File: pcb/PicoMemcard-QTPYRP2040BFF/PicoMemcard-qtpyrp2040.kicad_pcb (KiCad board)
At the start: 2 copper layers, 36.2 x 51.2 mm, 9 parts, among them J1 PSX Memory Card Interface, SW1 TS-1187A-B-A-B, SW2 TS-1187A-B-A-B, SW3 TS-1187A-B-A-B, U1 QT_PY_SD_BFF, U2 ADAFRUIT_QT_PY

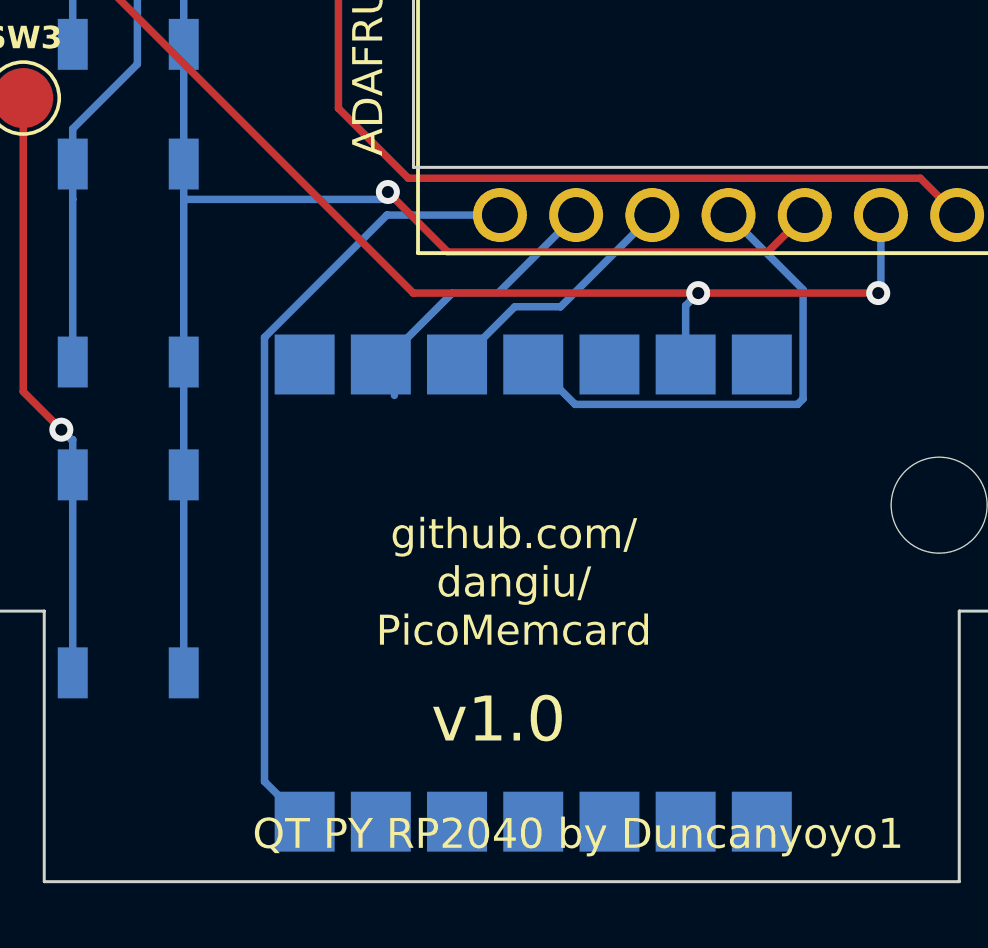
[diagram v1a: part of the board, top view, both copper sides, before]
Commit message: Connect 3V3 NET to MicroSD BFF
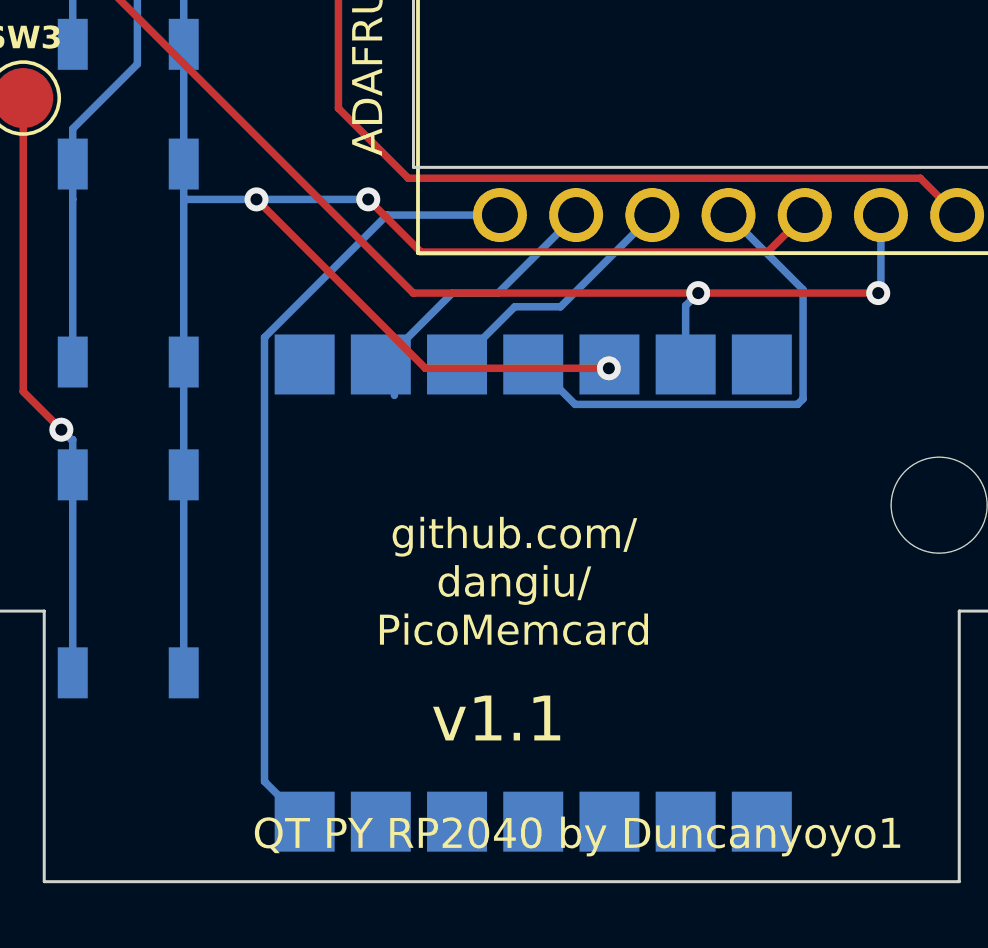
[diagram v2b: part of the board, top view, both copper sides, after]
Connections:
- U1 pad 12: +3.3V -> +3V3
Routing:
- net +3V3: track 49.7 -> 63.6 mm, vias 1 -> 3
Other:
- board text added: "v1.1"
- board text removed: "v1.0"
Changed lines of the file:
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@@
   (net 15 "MOSI")
   (net 16 "+3V3")
-  (net 17 "+3.3V")
   (footprint "MountingHole:MountingHole_3.2mm_M3" (layer "F.Cu")
     (at 163.53 102.07)
@@
     (pad "12" smd roundrect (at 7.62 2.54 90) (size 2 2) (layers "B.Cu" "B.Paste" "B.Mask") (roundrect_rratio 0.25)
       (chamfer_ratio 0) (chamfer top_left bottom_left)
-      (net 17 "+3.3V") (pinfunction "3V3") (pintype "power_in"))
+      (net 16 "+3V3") (pinfunction "3V3") (pintype "power_in"))
     (pad "13" smd roundrect (at 7.62 5.08 90) (size 2 2) (layers "B.Cu" "B.Paste" "B.Mask") (roundrect_rratio 0.25)
       (chamfer_ratio 0) (chamfer top_left bottom_left)
@@
     (effects (font (size 1 1) (thickness 0.22)))
   )
-  (gr_text "v1.0" (at 148.844 109.22) (layer "F.SilkS")
+  (gr_text "v1.1" (at 148.844 109.22) (layer "F.SilkS")
     (effects (font (size 1.5 1.5) (thickness 0.3)))
   )
@@
   (segment (start 158.994 94.8846) (end 156.509 92.3992) (width 0.25) (layer "B.Cu") (net 15))
   (segment (start 150.064 97.38) (end 150 97.38) (width 0.25) (layer "B.Cu") (net 15))
-  (segment (start 157.8149 93.6333) (end 147.1564 93.6333) (width 0.25) (layer "F.Cu") (net 16))
-  (segment (start 147.1564 93.6333) (end 145.154 91.6309) (width 0.25) (layer "F.Cu") (net 16))
-  (segment (start 159.049 92.3992) (end 157.8149 93.6333) (width 0.25) (layer "F.Cu") (net 16))
-  (via (at 145.154 91.6309) (size 0.8) (drill 0.4) (layers "F.Cu" "B.Cu") (net 16))
+  (segment (start 144.5 91.8769) (end 146.2564 93.6333) (width 0.25) (layer "F.Cu") (net 16))
+  (segment (start 140.774394 91.877634) (end 146.404406 97.507646) (width 0.25) (layer "F.Cu") (net 16))
+  (segment (start 157.8149 93.6333) (end 159.049 92.3992) (width 0.25) (layer "F.Cu") (net 16))
+  (segment (start 146.2564 93.6333) (end 157.8149 93.6333) (width 0.25) (layer "F.Cu") (net 16))
+  (segment (start 146.404406 97.507646) (end 152.520396 97.507646) (width 0.25) (layer "F.Cu") (net 16))
+  (via (at 140.774394 91.877634) (size 0.8) (drill 0.4) (layers "F.Cu" "B.Cu") (net 16))
+  (via (at 152.520396 97.507646) (size 0.8) (drill 0.4) (layers "F.Cu" "B.Cu") (net 16))
+  (via (at 144.5 91.8769) (size 0.8) (drill 0.4) (layers "F.Cu" "B.Cu") (net 16))
   (segment (start 138.35 80.11) (end 138.35 86.71) (width 0.25) (layer "B.Cu") (net 16))
+  (segment (start 140.77366 91.8769) (end 138.35 91.8769) (width 0.25) (layer "B.Cu") (net 16))
+  (segment (start 140.774394 91.877634) (end 140.77366 91.8769) (width 0.25) (layer "B.Cu") (net 16))
+  (segment (start 140.775128 91.8769) (end 144.5 91.8769) (width 0.25) (layer "B.Cu") (net 16))
   (segment (start 138.35 97.3) (end 138.35 101.06) (width 0.25) (layer "B.Cu") (net 16))
+  (segment (start 140.774394 91.877634) (end 140.775128 91.8769) (width 0.25) (layer "B.Cu") (net 16))
   (segment (start 138.35 90.7) (end 138.35 91.8769) (width 0.25) (layer "B.Cu") (net 16))
-  (segment (start 144.908 91.8769) (end 138.35 91.8769) (width 0.25) (layer "B.Cu") (net 16))
-  (segment (start 145.154 91.6309) (end 144.908 91.8769) (width 0.25) (layer "B.Cu") (net 16))
   (segment (start 138.35 91.8769) (end 138.35 97.3) (width 0.25) (layer "B.Cu") (net 16))
   (segment (start 138.35 86.71) (end 138.35 90.7) (width 0.25) (layer "B.Cu") (net 16))

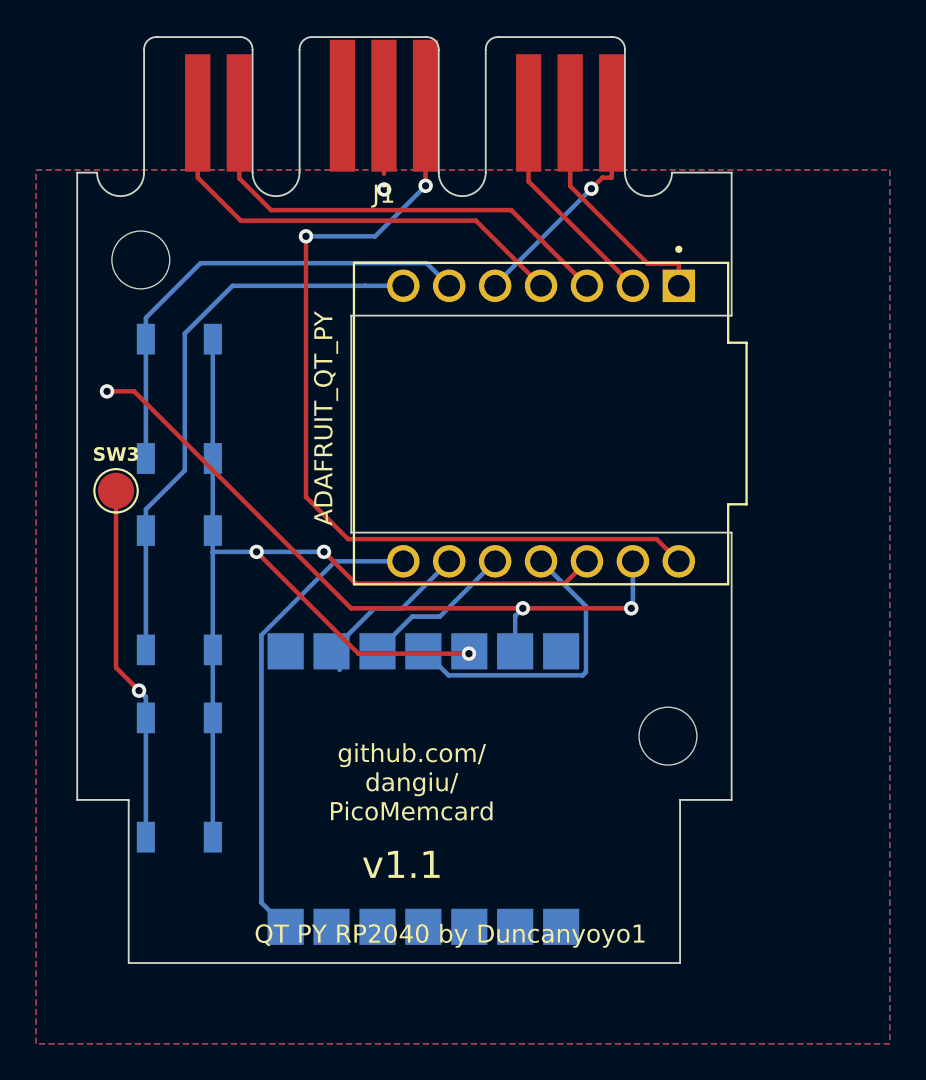
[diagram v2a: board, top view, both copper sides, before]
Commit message: Fix QTPY MicroSD BFF Footprint
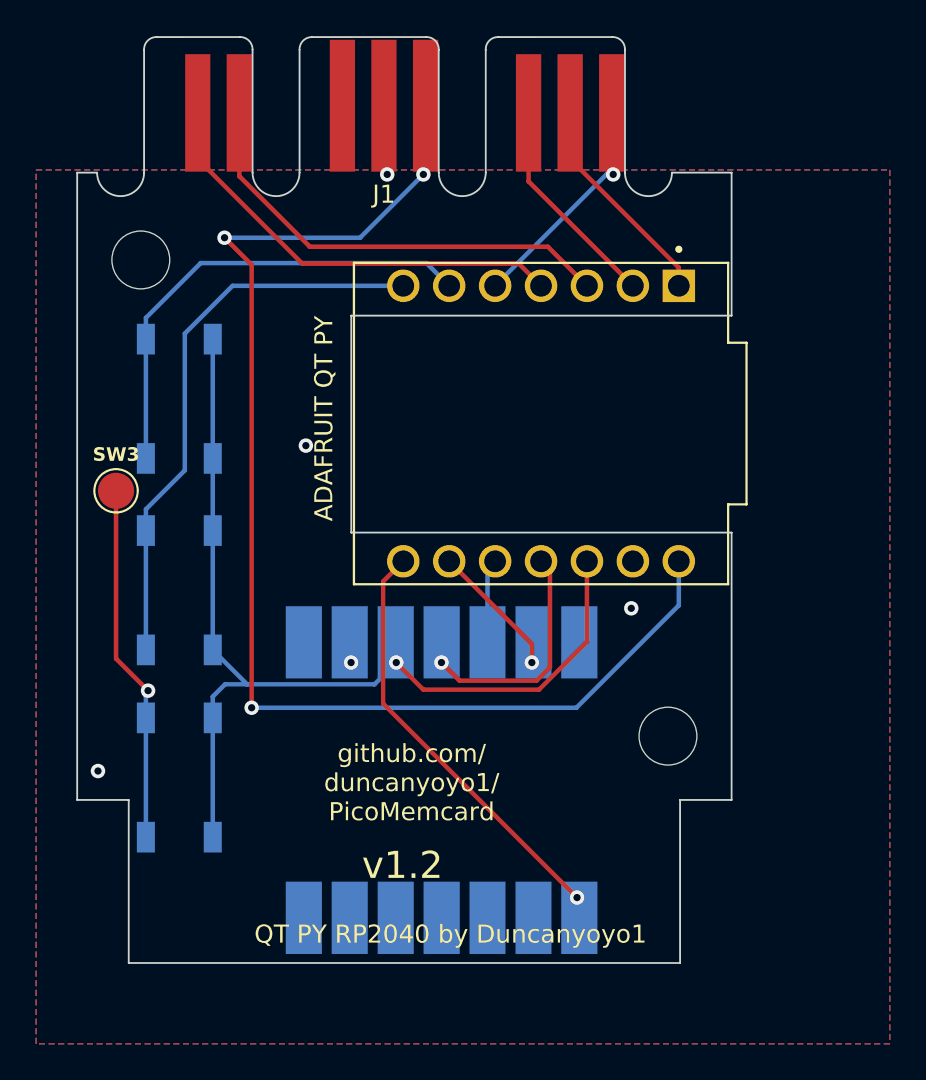
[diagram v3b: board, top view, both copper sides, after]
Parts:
- U1: value QT_PY_SD_BFF -> QT PY SD BFF
- U2: value ADAFRUIT_QT_PY -> ADAFRUIT QT PY
- moved U1 1.13 mm to (151.0, 104.5), turned to -90 degrees
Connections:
- U1 pad 10: MISO -> (no net)
- U1 pad 11: MOSI -> (no net)
- U1 pad 12: +3V3 -> (no net)
- U1 pad 13: GND -> (no net)
- U1 pad 14: (no net) -> CS
- U1 pad 2: (no net) -> SCK
- U1 pad 3: (no net) -> MISO
- U1 pad 4: (no net) -> MOSI
- U1 pad 5: (no net) -> +3V3
- U1 pad 6: (no net) -> GND
- U1 pad 7: CS -> (no net)
- U1 pad 9: SCK -> (no net)
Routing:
- net GND: track 43.0 -> 3.87 mm, vias 4 -> 5
- net +5V: track 48.7 -> 71.3 mm, vias 2 -> 3
- net +3V3: track 63.6 -> 56.4 mm, vias 3 -> 1
- net MISO: track 8.57 -> 4.66 mm
- net MOSI: track 17.7 -> 13.9 mm, vias 0 -> 1
- net SCK: track 11.0 -> 8.65 mm, vias 0 -> 1
- net CS: track 26.2 -> 24.7 mm, vias 0 -> 1
- net CLK: track 13.1 -> 12.0 mm
- net DAT: track 25.0 -> 24.4 mm
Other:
- board text added: "github.com/ duncanyoyo1/ PicoMemcard"
- board text added: "v1.2"
- board text removed: "github.com/ dangiu/ PicoMemcard"
- board text removed: "v1.1"
